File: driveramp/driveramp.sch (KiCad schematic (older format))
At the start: 86 parts, among them J1 SMA, J2 SMA, K1 CONN_3, P2 CONN_2, Q1 BC547BTA, T1 MABACT0067, T2 2x Fair-Rite 2843006802, coax, U1 ISL43210A, U2 MRFE6VP100H, U3 LM317HV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

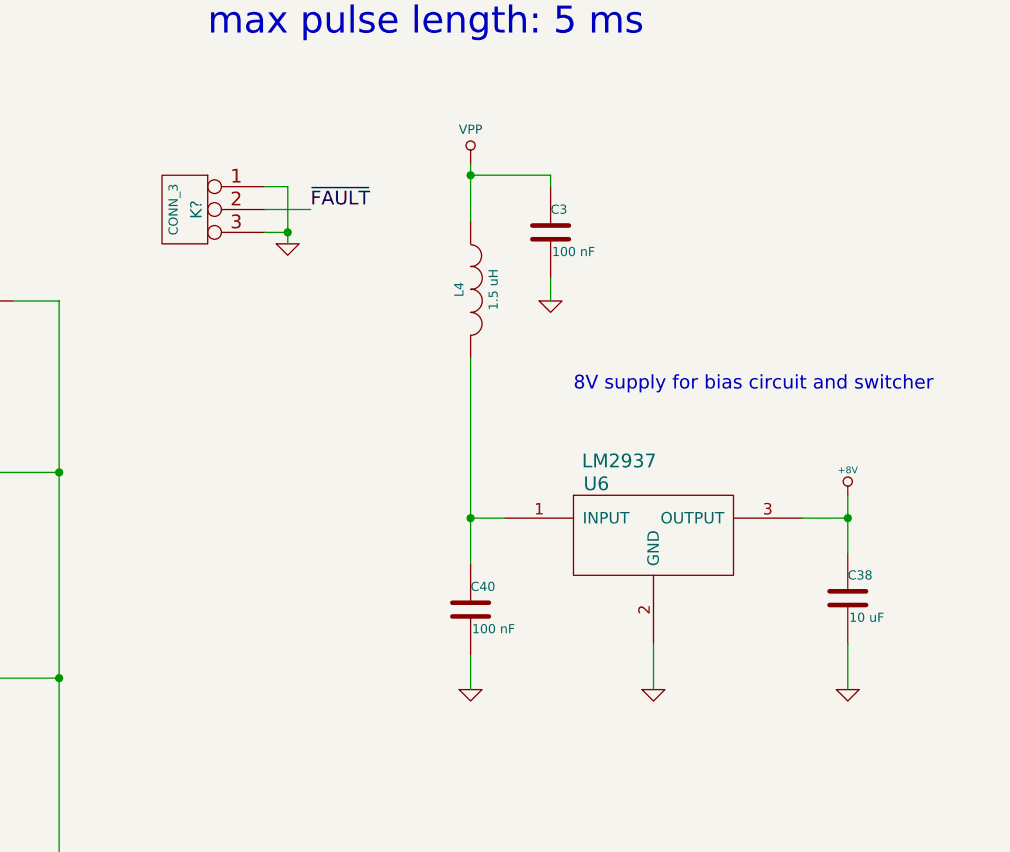
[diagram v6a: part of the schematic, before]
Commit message: changed 8v regulator on driver amp for fault shutdown
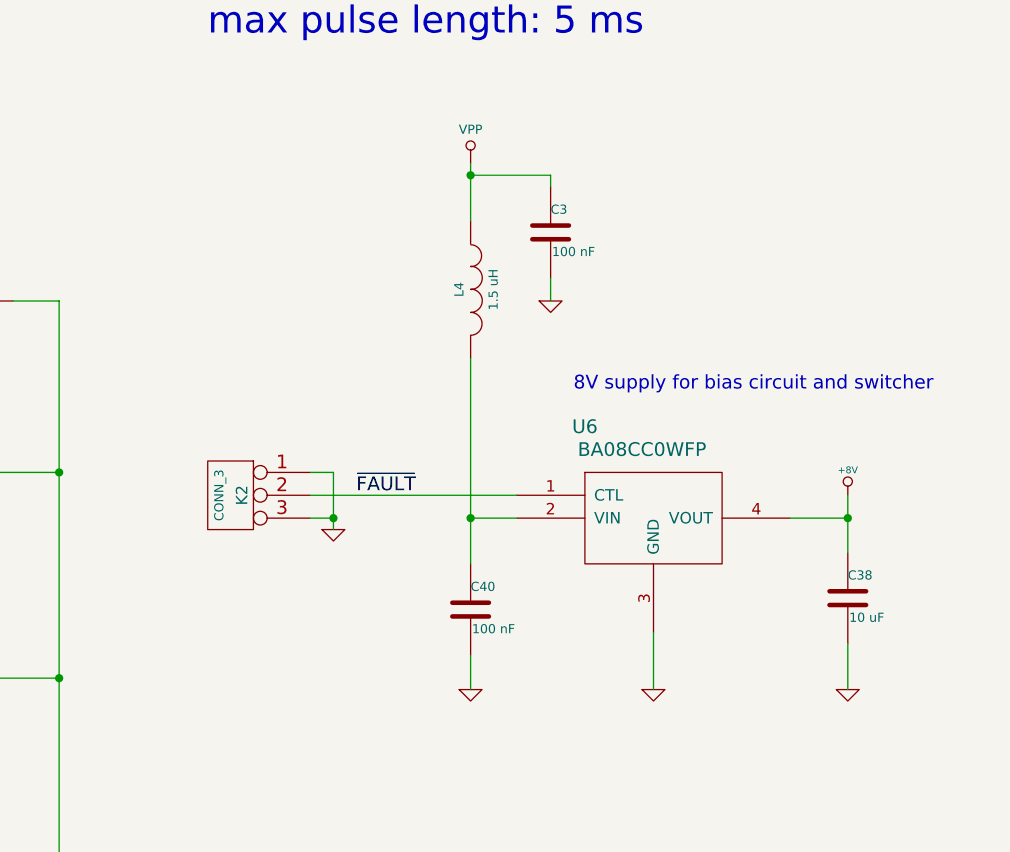
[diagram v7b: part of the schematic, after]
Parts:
- removed U6: LM2937, SMD_Packages:SOT-223, symbol LM2937
- added U6: BA08CC0WFP, to252_5:TO252-5, symbol BA08CC0WFP
- C4: footprint SMD_Packages:SMD-0805 -> SMD_Packages:SMD-1210
- JP1, K1: footprint localconn:3-647166-3 -> sdtransmitter:0740991003
- K2: renamed from K?; footprint localconn:3-647166-3 -> sdtransmitter:0740991003
- R17: footprint SMD_Packages:SMD-0805 -> SMD_Packages:SMD-2512_Pol
- U1: footprint Transistors_SMD:sc70-6 -> SMD_Packages:SOT-23-6
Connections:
- net +8V: now also U6.4 (VOUT)
- net GND: now also U6.3 (GND)
- net ~FAULT: now also U6.1 (CTL)
- net at C40.1, L4.2: now also U6.2 (VIN)
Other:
- moved on the sheet: K2
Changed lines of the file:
@@
 LIBS:lm2937
 LIBS:pe4239
+LIBS:ba08cc0wfp
 LIBS:driveramp-cache
 EELAYER 24 0
@@
 P15449CT-ND
 $Comp
-L GND #PWR14
+L GND #PWR13
 U 1 1 53A8EFAD
 P 2950 10500
-F 0 "#PWR14" H 2950 10500 30  0001 C CNN
+F 0 "#PWR13" H 2950 10500 30  0001 C CNN
 F 1 "GND" H 2950 10430 30  0001 C CNN
 F 2 "" H 2950 10500 60  0000 C CNN
@@
 $EndComp
 $Comp
-L GND #PWR25
+L GND #PWR24
 U 1 1 53A8F194
 P 4350 8800
-F 0 "#PWR25" H 4350 8800 30  0001 C CNN
+F 0 "#PWR24" H 4350 8800 30  0001 C CNN
 F 1 "GND" H 4350 8730 30  0001 C CNN
 F 2 "" H 4350 8800 60  0000 C CNN
@@
 F 0 "C4" H 11600 8100 40  0000 L CNN
 F 1 "DNP" H 11606 7915 40  0000 L CNN
-F 2 "SMD_Packages:SMD-0805" H 11638 7850 30  0001 C CNN
+F 2 "SMD_Packages:SMD-1210" H 11638 7850 30  0001 C CNN
 F 3 "~" H 11600 8000 60  0000 C CNN
 	1    11600 8000
@@
 F 0 "U1" H 2700 5400 60  0000 C CNN
 F 1 "ISL43210A" H 2800 5500 60  0000 C CNN
-F 2 "Transistors_SMD:sc70-6" H 2900 5100 60  0001 C CNN
+F 2 "SMD_Packages:SOT-23-6" H 2900 5100 60  0001 C CNN
 F 3 "" H 2900 5100 60  0000 C CNN
 	1    2900 5100
@@
 $EndComp
 $Comp
-L GND #PWR29
+L GND #PWR28
 U 1 1 54AC8E4C
 P 4700 2700
-F 0 "#PWR29" H 4700 2700 30  0001 C CNN
+F 0 "#PWR28" H 4700 2700 30  0001 C CNN
 F 1 "GND" H 4700 2630 30  0001 C CNN
 F 2 "" H 4700 2700 60  0000 C CNN
@@
 $EndComp
 $Comp
-L +8V #PWR28
+L +8V #PWR27
 U 1 1 54AC8F02
 P 4700 950
-F 0 "#PWR28" H 4700 920 20  0001 C CNN
+F 0 "#PWR27" H 4700 920 20  0001 C CNN
 F 1 "+8V" H 4700 1060 30  0000 C CNN
 F 2 "" H 4700 950 60  0000 C CNN
@@
 $EndComp
 $Comp
-L GND #PWR31
+L GND #PWR30
 U 1 1 54AC8FAE
 P 5000 1550
-F 0 "#PWR31" H 5000 1550 30  0001 C CNN
+F 0 "#PWR30" H 5000 1550 30  0001 C CNN
 F 1 "GND" H 5000 1480 30  0001 C CNN
 F 2 "" H 5000 1550 60  0000 C CNN
@@
 $EndComp
 $Comp
-L GND #PWR21
+L GND #PWR20
 U 1 1 54AC9305
 P 4000 3500
-F 0 "#PWR21" H 4000 3500 30  0001 C CNN
+F 0 "#PWR20" H 4000 3500 30  0001 C CNN
 F 1 "GND" H 4000 3430 30  0001 C CNN
 F 2 "" H 4000 3500 60  0000 C CNN
@@
 $EndComp
 $Comp
-L GND #PWR24
+L GND #PWR23
 U 1 1 54AC9B2E
 P 4300 5700
-F 0 "#PWR24" H 4300 5700 30  0001 C CNN
+F 0 "#PWR23" H 4300 5700 30  0001 C CNN
 F 1 "GND" H 4300 5630 30  0001 C CNN
 F 2 "" H 4300 5700 60  0000 C CNN
@@
 $EndComp
 $Comp
-L GND #PWR27
+L GND #PWR26
 U 1 1 54AC9CAC
 P 4600 5700
-F 0 "#PWR27" H 4600 5700 30  0001 C CNN
+F 0 "#PWR26" H 4600 5700 30  0001 C CNN
 F 1 "GND" H 4600 5630 30  0001 C CNN
 F 2 "" H 4600 5700 60  0000 C CNN
@@
 $EndComp
 $Comp
-L GND #PWR18
+L GND #PWR17
 U 1 1 54AC9D98
 P 3500 5900
-F 0 "#PWR18" H 3500 5900 30  0001 C CNN
+F 0 "#PWR17" H 3500 5900 30  0001 C CNN
 F 1 "GND" H 3500 5830 30  0001 C CNN
 F 2 "" H 3500 5900 60  0000 C CNN
@@
 $EndComp
 $Comp
-L GND #PWR30
+L GND #PWR29
 U 1 1 54ACA1B8
 P 4700 4400
-F 0 "#PWR30" H 4700 4400 30  0001 C CNN
+F 0 "#PWR29" H 4700 4400 30  0001 C CNN
 F 1 "GND" H 4700 4330 30  0001 C CNN
 F 2 "" H 4700 4400 60  0000 C CNN
@@
 $EndComp
 $Comp
-L GND #PWR26
+L GND #PWR25
 U 1 1 54ACA1C3
 P 4450 4400
-F 0 "#PWR26" H 4450 4400 30  0001 C CNN
+F 0 "#PWR25" H 4450 4400 30  0001 C CNN
 F 1 "GND" H 4450 4330 30  0001 C CNN
 F 2 "" H 4450 4400 60  0000 C CNN
@@
 $EndComp
 $Comp
-L GND #PWR23
+L GND #PWR21
 U 1 1 54ACA1CE
 P 4150 4400
-F 0 "#PWR23" H 4150 4400 30  0001 C CNN
+F 0 "#PWR21" H 4150 4400 30  0001 C CNN
 F 1 "GND" H 4150 4330 30  0001 C CNN
 F 2 "" H 4150 4400 60  0000 C CNN
@@
 $EndComp
 $Comp
-L GND #PWR20
+L GND #PWR18
 U 1 1 54ACA1D9
 P 3850 4400
-F 0 "#PWR20" H 3850 4400 30  0001 C CNN
+F 0 "#PWR18" H 3850 4400 30  0001 C CNN
 F 1 "GND" H 3850 4330 30  0001 C CNN
 F 2 "" H 3850 4400 60  0000 C CNN
@@
 $EndComp
 $Comp
-L GND #PWR11
+L GND #PWR10
 U 1 1 54ACAB43
 P 2300 5400
-F 0 "#PWR11" H 2300 5400 30  0001 C CNN
+F 0 "#PWR10" H 2300 5400 30  0001 C CNN
 F 1 "GND" H 2300 5330 30  0001 C CNN
 F 2 "" H 2300 5400 60  0000 C CNN
@@
 F 0 "K1" V 750 3900 50  0000 C CNN
 F 1 "CONN_3" V 850 3900 40  0000 C CNN
-F 2 "localconn:3-647166-3" H 800 3900 60  0001 C CNN
+F 2 "sdtransmitter:0740991003" H 800 3900 60  0001 C CNN
 F 3 "" H 800 3900 60  0000 C CNN
 	1    800  3900
@@
 $EndComp
 $Comp
-L GND #PWR9
+L GND #PWR8
 U 1 1 54ACADE3
 P 2000 5700
-F 0 "#PWR9" H 2000 5700 30  0001 C CNN
+F 0 "#PWR8" H 2000 5700 30  0001 C CNN
 F 1 "GND" H 2000 5630 30  0001 C CNN
 F 2 "" H 2000 5700 60  0000 C CNN
@@
 $EndComp
 $Comp
-L GND #PWR13
+L GND #PWR12
 U 1 1 54ACB9E7
 P 2500 3900
-F 0 "#PWR13" H 2500 3900 30  0001 C CNN
+F 0 "#PWR12" H 2500 3900 30  0001 C CNN
 F 1 "GND" H 2500 3830 30  0001 C CNN
 F 2 "" H 2500 3900 60  0000 C CNN
@@
 $EndComp
 $Comp
-L GND #PWR10
+L GND #PWR9
 U 1 1 54ACB9F2
 P 2250 3900
-F 0 "#PWR10" H 2250 3900 30  0001 C CNN
+F 0 "#PWR9" H 2250 3900 30  0001 C CNN
 F 1 "GND" H 2250 3830 30  0001 C CNN
 F 2 "" H 2250 3900 60  0000 C CNN
@@
 $EndComp
 $Comp
-L +8V #PWR12
+L +8V #PWR11
 U 1 1 54ACBD74
 P 2500 1150
-F 0 "#PWR12" H 2500 1120 20  0001 C CNN
+F 0 "#PWR11" H 2500 1120 20  0001 C CNN
 F 1 "+8V" H 2500 1260 30  0000 C CNN
 F 2 "" H 2500 1150 60  0000 C CNN
@@
 $EndComp
 $Comp
-L GND #PWR16
+L GND #PWR14
 U 1 1 54ACC3C9
 P 3150 3900
-F 0 "#PWR16" H 3150 3900 30  0001 C CNN
+F 0 "#PWR14" H 3150 3900 30  0001 C CNN
 F 1 "GND" H 3150 3830 30  0001 C CNN
 F 2 "" H 3150 3900 60  0000 C CNN
@@
 $EndComp
 $Comp
-L GND #PWR17
+L GND #PWR16
 U 1 1 54ACC5BF
 P 3400 2600
-F 0 "#PWR17" H 3400 2600 30  0001 C CNN
+F 0 "#PWR16" H 3400 2600 30  0001 C CNN
 F 1 "GND" H 3400 2530 30  0001 C CNN
 F 2 "" H 3400 2600 60  0000 C CNN
@@
 $EndComp
 $Comp
-L GND #PWR32
+L GND #PWR31
 U 1 1 54AF1280
 P 5600 7400
-F 0 "#PWR32" H 5600 7400 30  0001 C CNN
+F 0 "#PWR31" H 5600 7400 30  0001 C CNN
 F 1 "GND" H 5600 7330 30  0001 C CNN
 F 2 "" H 5600 7400 60  0000 C CNN
@@
 F 0 "R17" V 3930 6700 40  0000 C CNN
 F 1 "43.2" V 4000 6700 40  0000 C CNN
-F 2 "SMD_Packages:SMD-0805" V 3780 6700 30  0001 C CNN
+F 2 "SMD_Packages:SMD-2512_Pol" V 3780 6700 30  0001 C CNN
 F 3 "" H 3850 6700 30  0000 C CNN
 	1    3850 6700
@@
 $EndComp
 $Comp
-L LM2937 U6
-U 1 1 54CABE47
-P 8000 3050
-F 0 "U6" H 7750 3200 60  0000 C CNN
-F 1 "LM2937" H 7850 3300 60  0000 C CNN
-F 2 "SMD_Packages:SOT-223" H 8000 3050 60  0001 C CNN
-F 3 "" H 8000 3050 60  0000 C CNN
-	1    8000 3050
-	1    0    0    -1
-$EndComp
-$Comp
 L GND #PWR38
 U 1 1 54CAC109
@@
 F 0 "JP1" H 5450 5000 40  0000 L CNN
 F 1 "JUMPER3" H 5400 5200 40  0000 C CNN
-F 2 "localconn:3-647166-3" H 5400 5100 60  0001 C CNN
+F 2 "sdtransmitter:0740991003" H 5400 5100 60  0001 C CNN
 F 3 "" H 5400 5100 60  0000 C CNN
 	1    5400 5100
@@
 $EndComp
 $Comp
-L CONN_3 K?
+L CONN_3 K2
 U 1 1 54D41668
-P 5950 1700
-F 0 "K?" V 5900 1700 50  0000 C CNN
-F 1 "CONN_3" V 6000 1700 40  0000 C CNN
-F 2 "localconn:3-647166-3" H 5950 1700 60  0001 C CNN
-F 3 "" H 5950 1700 60  0000 C CNN
-	1    5950 1700
+P 6150 2950
+F 0 "K2" V 6100 2950 50  0000 C CNN
+F 1 "CONN_3" V 6200 2950 40  0000 C CNN
+F 2 "sdtransmitter:0740991003" H 6150 2950 60  0001 C CNN
+F 3 "" H 6150 2950 60  0000 C CNN
+	1    6150 2950
 	-1   0    0    -1
 $EndComp
-Text Label 6500 1700 0    60   ~ 0
+Text Label 6700 2950 0    60   ~ 0
 ~FAULT
 $Comp
-L GND #PWR?
+L GND #PWR32
 U 1 1 54D4183E
-P 6400 1850
-F 0 "#PWR?" H 6400 1850 30  0001 C CNN
-F 1 "GND" H 6400 1780 30  0001 C CNN
-F 2 "" H 6400 1850 60  0000 C CNN
-F 3 "" H 6400 1850 60  0000 C CNN
-	1    6400 1850
+P 6600 3100
+F 0 "#PWR32" H 6600 3100 30  0001 C CNN
+F 1 "GND" H 6600 3030 30  0001 C CNN
+F 2 "" H 6600 3100 60  0000 C CNN
+F 3 "" H 6600 3100 60  0000 C CNN
+	1    6600 3100
 	1    0    0    -1
 $EndComp
@@
 	8850 3600 8850 3800
 Wire Wire Line
-	8650 3050 8850 3050
-Wire Wire Line
-	8000 3800 8000 3600
-Wire Wire Line
-	7350 3050 7200 3050
+	8600 3050 8850 3050
+Wire Wire Line
+	8000 3550 8000 3800
+Wire Wire Line
+	7200 3050 7400 3050
 Connection ~ 7200 3050
 Wire Wire Line
@@
 	5400 5200 5400 5400
 Wire Wire Line
-	6300 1700 6500 1700
-Wire Wire Line
-	6300 1800 6400 1800
-Wire Wire Line
-	6400 1600 6400 1850
-Wire Wire Line
-	6300 1600 6400 1600
-Connection ~ 6400 1800
+	6500 2950 7400 2950
+Wire Wire Line
+	6500 3050 6600 3050
+Wire Wire Line
+	6600 2850 6600 3100
+Wire Wire Line
+	6500 2850 6600 2850
+Connection ~ 6600 3050
 Wire Wire Line
 	4350 7750 4450 7750
@@
 Wire Wire Line
 	1600 7750 2200 7750
+$Comp
+L BA08CC0WFP U6
+U 1 1 54D4286C
+P 8000 3050
+F 0 "U6" H 7700 3450 60  0000 C CNN
+F 1 "BA08CC0WFP" H 7950 3350 60  0000 C CNN
+F 2 "to252_5:TO252-5" H 8000 3050 60  0001 C CNN
+F 3 "" H 8000 3050 60  0000 C CNN
+	1    8000 3050
+	1    0    0    -1
+$EndComp
 $EndSCHEMATC

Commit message: DFM changes..
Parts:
- added R9: 1.1k 1%, SMD_Packages:SMD-0603, symbol R
- C1, C18, C19, C2, C25, C27, C32, C41, C7, C8: value 22nF -> 22 nF
- C10: value JMP -> 22 nF; footprint SMD_Packages:SMD-1210 -> SMD_Packages:SMD-0805
- JP1: value JUMPER3 -> SMD_HDR
- K1, K2: value CONN_3 -> SMD_HDR
- R10: value 2k 1% -> 909 1%
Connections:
- net at C13.1, R14.2, U4.3 (+IN): now also R10.2; no longer R10.1
- net at RV1.2: now also R9.1; no longer R10.2
- new net: R10.1, R9.2
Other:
- moved on the sheet: RV1
